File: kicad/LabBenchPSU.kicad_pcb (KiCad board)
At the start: 2 copper layers, 150 x 96 mm, 14 parts, among them J1 ATX-24, J10 V+, J11 GND, J12 Solder Gnd, J13 Solder 12V, J2 GND, J3 GND, J4 +12V, J5 +5V, J6 +3.3V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

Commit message: add affiliate links
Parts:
- moved J1 74.7 mm to (73.7, 88.9), turned to 0 degrees
- moved SW1 61.2 mm to (84.8, 78.2), turned to 90 degrees
- moved J13 50.8 mm to (127.3, 88.6)
- moved J8 39.5 mm to (123.8, 66.2), turned to 270 degrees
- moved J9 37.1 mm to (129.5, 52.8)
- moved J12 20.7 mm to (118.1, 55.6), turned to 90 degrees
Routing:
- net Net-(J1-Pad10): track 215.8 -> 72.3 mm
- net Net-(J1-Pad16): track 32.6 -> 7.06 mm
- net Net-(J1-Pad21): track 102.1 -> 78.0 mm, vias 13 -> 0
- net /VOUT+: track 32.8 -> 10.7 mm
- net /VOUT-: track 15.2 -> 34.2 mm
- net /VIN+: track 26.5 -> 44.0 mm
- net Net-(J1-Pad1): track 67.0 -> 55.5 mm
- net /VIN-: track 35.0 -> 45.9 mm
- net Net-(J1-Pad14): track 102.8 -> 112.0 mm, vias 6 -> 0
- net Net-(J1-Pad15): track 231.7 -> 235.6 mm
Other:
- board size 150 x 96 mm -> 125 x 49.6 mm
- board text added: "-12V"
- board text added: "12V"
- board text added: "3.3V"
- board text added: "5V"
- board text added: "GND"
- board text added: "OUT+"
- board text added: "OUT-"
- board text added: "Solder Jumper 12V"
- board text added: "Solder Jumper GND"
- board text added: "VIN+"
- board text added: "VIN-"
- board text added: "VOUT+"
- board text added: "VOUT-"

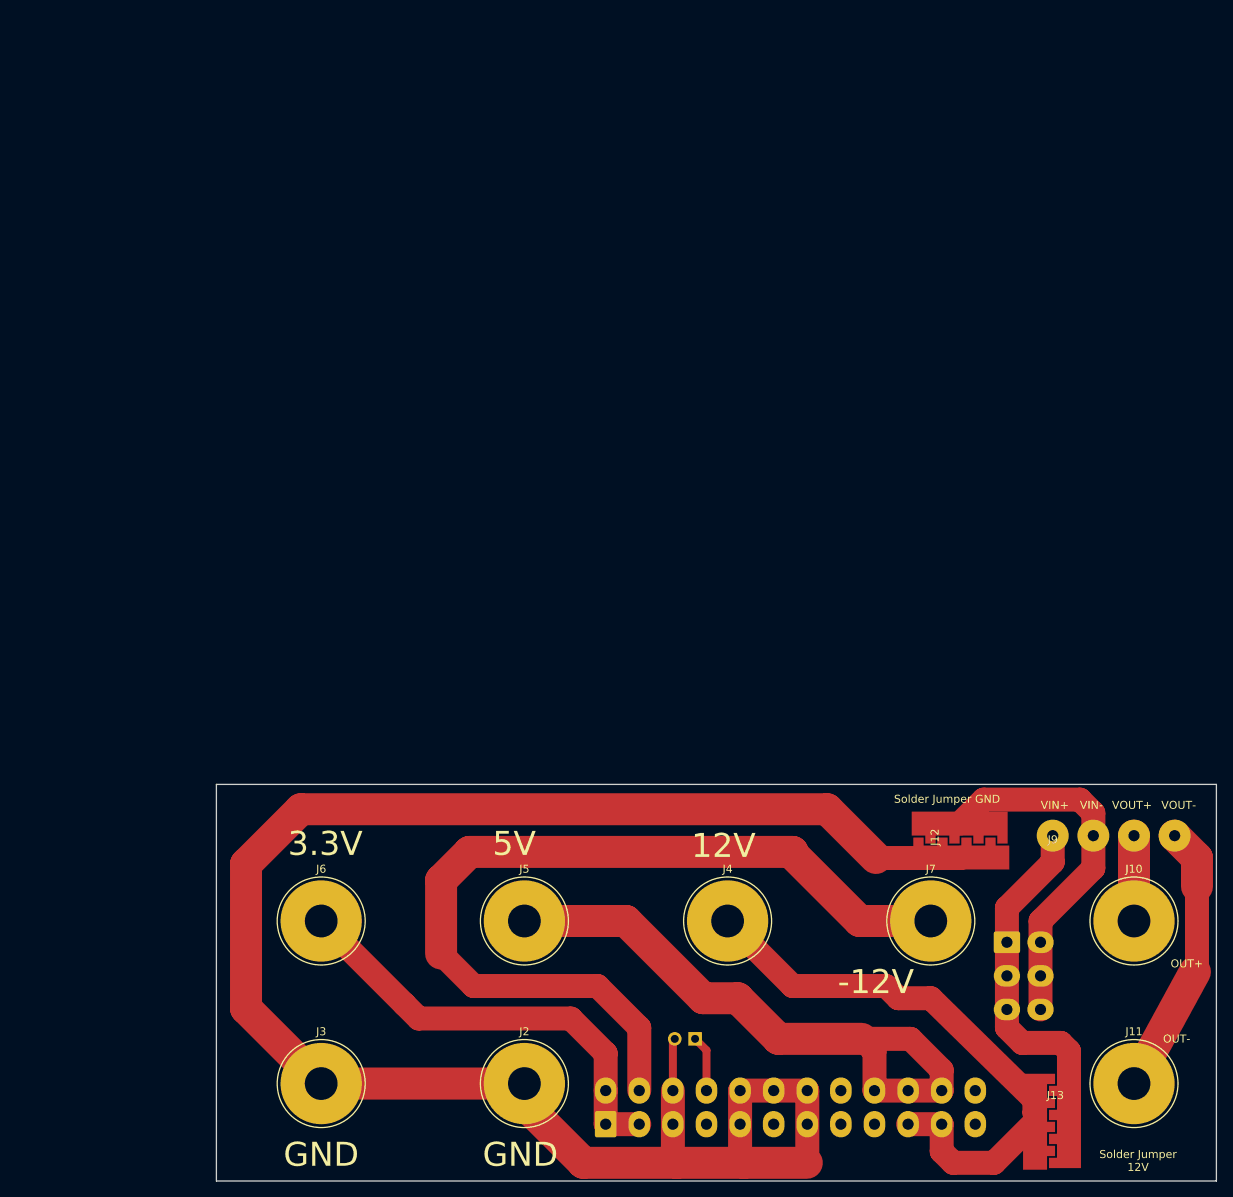
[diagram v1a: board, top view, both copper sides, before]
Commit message: - remove PCB support from front panel - shorten slot in front panel - reduce wall thickness to 2mm - refactor front panel positioning - add license
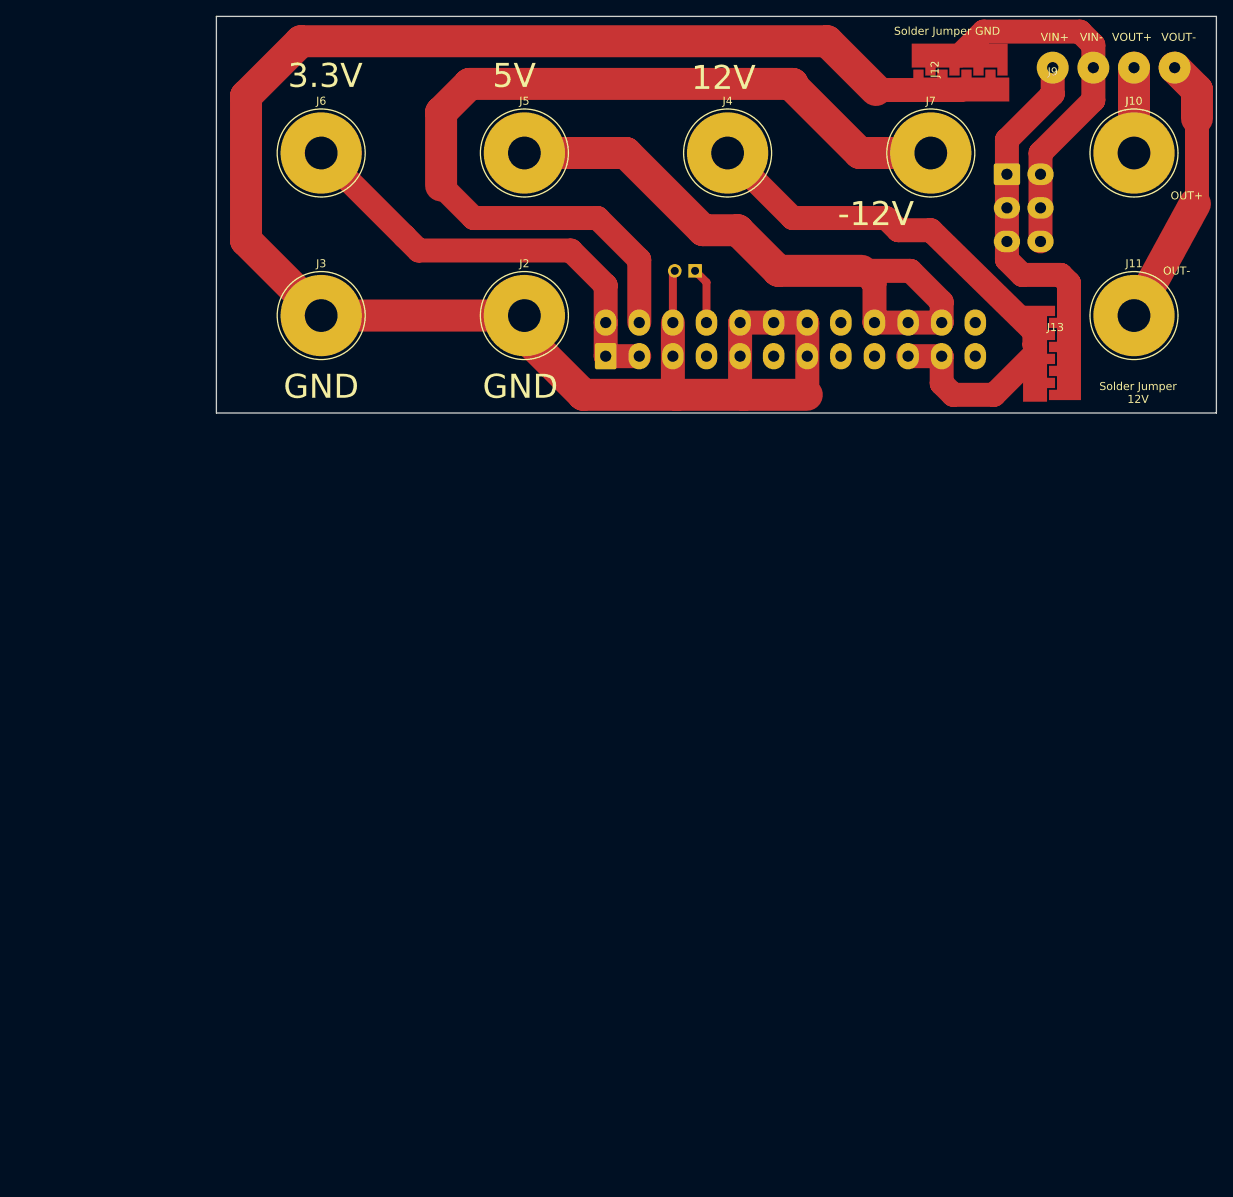
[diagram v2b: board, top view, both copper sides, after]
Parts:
- moved J1 96.0 mm to (73.7, -7.10)
- moved J10 96.0 mm to (139.7, -32.5)
- moved J11 96.0 mm to (139.7, -12.2)
- moved J12 96.0 mm to (118.1, -40.4)
- moved J13 96.0 mm to (127.3, -7.41)
- moved J2 96.0 mm to (63.5, -12.2)
- moved J3 96.0 mm to (38.1, -12.2)
- moved J4 96.0 mm to (88.9, -32.5)
- moved J5 96.0 mm to (63.5, -32.5)
- moved J6 96.0 mm to (38.1, -32.5)
- moved J7 96.0 mm to (114.3, -32.5)
- moved J8 96.0 mm to (123.8, -29.8)
- moved J9 96.0 mm to (129.5, -43.2)
- moved SW1 96.0 mm to (84.8, -17.8)

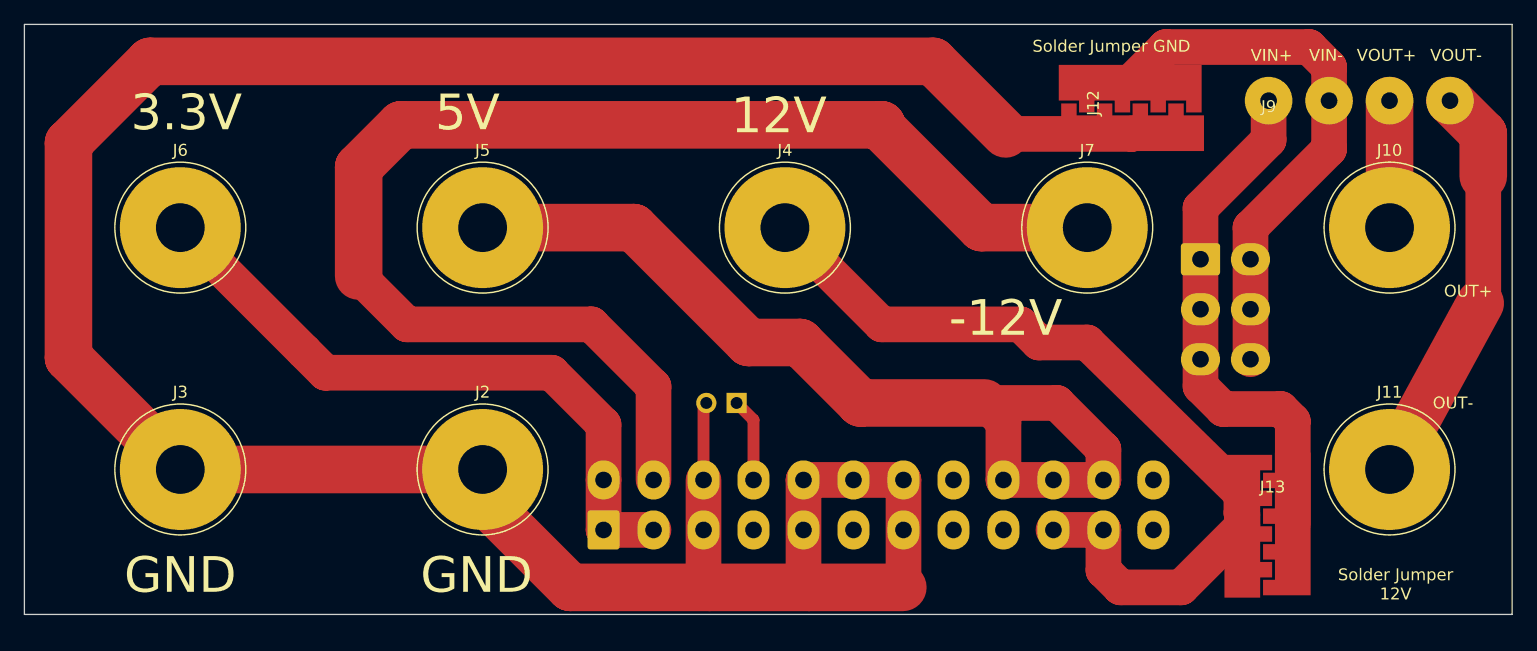
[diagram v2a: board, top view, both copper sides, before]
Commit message: make board double sided
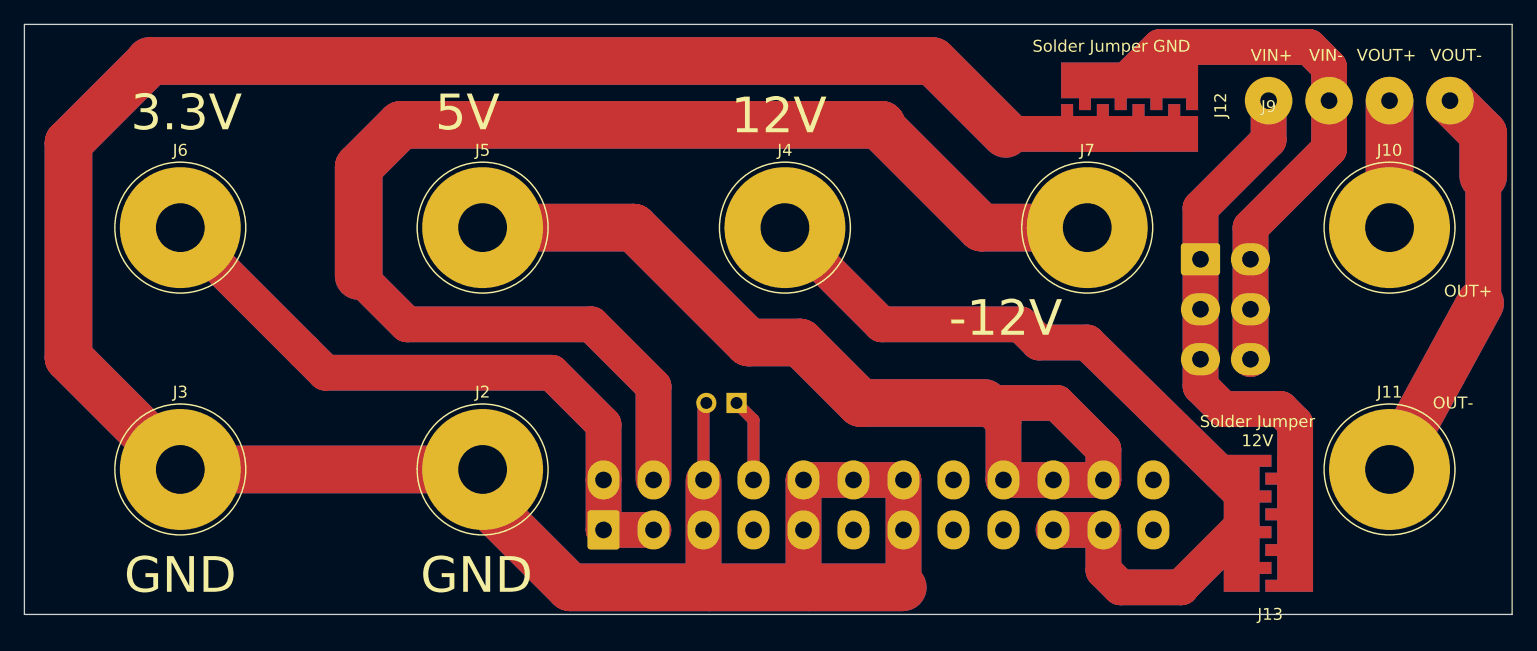
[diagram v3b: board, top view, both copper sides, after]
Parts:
- J12, J13: footprint Footprints:High-Power-Solder-Jumper -> Footprints:High-Power-Solder-Jumper-Double-Sided
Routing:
- net Net-(J1-Pad15): track 235.6 -> 471.0 mm
- net Net-(J1-Pad14): track 112.0 -> 224.1 mm
- net Net-(J1-Pad21): track 78.0 -> 155.9 mm
- net Net-(J1-Pad10): track 72.3 -> 139.0 mm
- net Net-(J1-Pad1): track 55.5 -> 110.9 mm
- net /VIN-: track 45.9 -> 92.3 mm
- net /VIN+: track 44.0 -> 87.5 mm
- net /VOUT-: track 34.2 -> 68.4 mm
- net /VOUT+: track 10.7 -> 21.3 mm
- net Net-(J1-Pad16): track 7.06 -> 14.1 mm
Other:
- board text added: "Power Switch"
